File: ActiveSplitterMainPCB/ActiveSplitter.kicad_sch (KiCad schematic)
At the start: 24 parts, among them J1 SMA_EDGE, J2 SMA_EDGE, J3 SMA_EDGE, J4 SMA_EDGE, J5 SMA_EDGE, J6 Conn_01x28_Pin, J7 Conn_01x28_Pin, J8 Conn_01x12_Pin, J9 Conn_01x12_Pin, U1 PSA4-5043

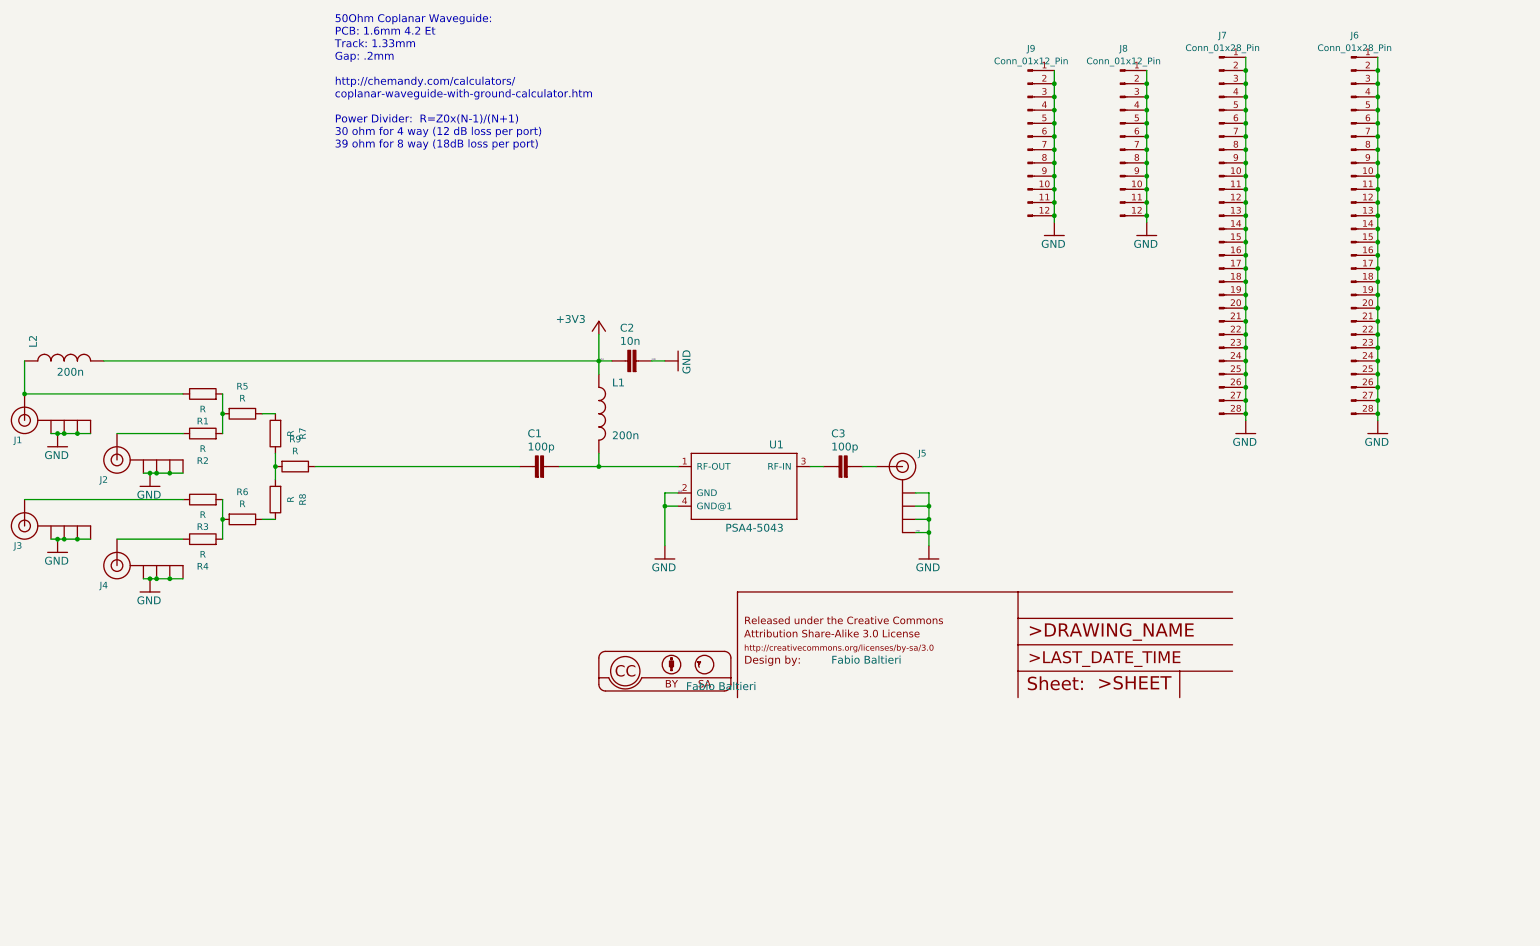
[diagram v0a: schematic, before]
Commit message: add termination resistors, PDF and SVG outputs for viewing
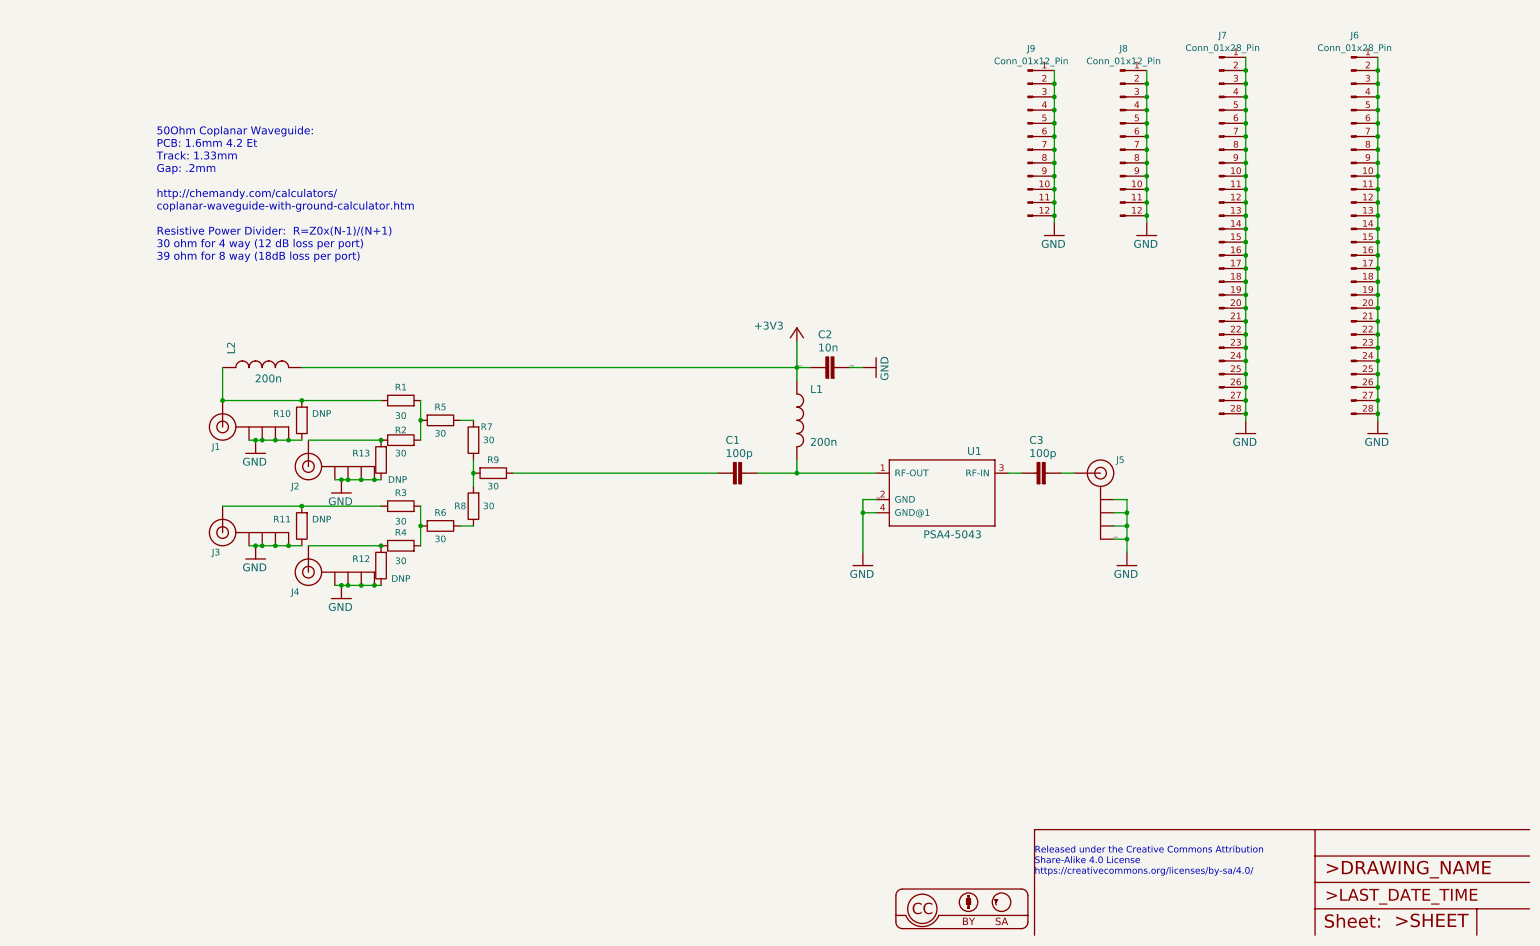
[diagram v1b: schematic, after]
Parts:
- added R10, R11, R12, R13: DNP, Resistor_SMD:R_0603_1608Metric_Pad0.98x0.95mm_HandSolder, symbol Device:R
- R1, R2, R3, R4, R5, R6, R7, R8, R9: value R -> 30
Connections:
- net GND: now also R10.1, R11.1, R12.1, R13.1
- net at J1.1 (SIGNAL), L2.1, R1.1: now also R10.2
- net at J3.1 (SIGNAL), R3.1: now also R11.2
- net at J4.1 (SIGNAL), R4.1: now also R12.2
- net at J2.1 (SIGNAL), R2.1: now also R13.2
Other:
- note added: "50Ohm Coplanar Waveguide: PCB: 1.6mm 4.2 Et Track: 1.33mm Gap: .2mm http://chemandy.com/calculators/ coplanar-waveguide-with-ground-calculator.htm Resistive Power Divider: R=Z0x(N-1)/(N+1) 30 ohm for 4 way (12 dB loss per port) 39 ohm for 8 way (18dB loss per port)"
- note added: "Released under the Creative Commons Attribution Share-Alike 4.0 License https://creativecommons.org/licenses/by-sa/4.0/"
- note removed: "50Ohm Coplanar Waveguide: PCB: 1.6mm 4.2 Et Track: 1.33mm Gap: .2mm http://chemandy.com/calculators/ coplanar-waveguide-with-ground-calculator.htm Power Divider: R=Z0x(N-1)/(N+1) 30 ohm for 4 way (12 dB loss per port) 39 ohm for 8 way (18dB loss per port)"
- moved on the sheet: C1, C2, C3, J1, J2, J3, J4, J5, L1, L2, R1, R2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

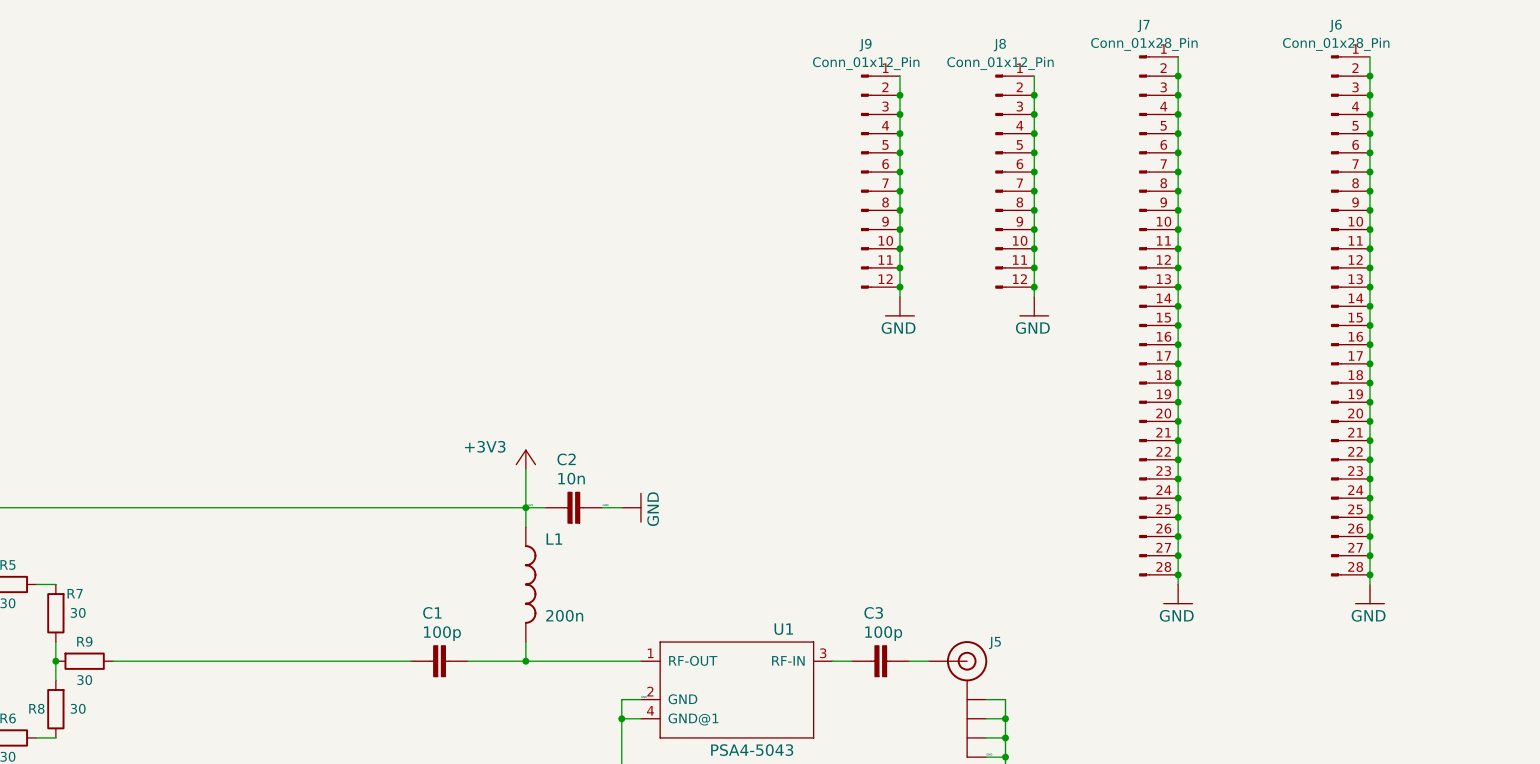
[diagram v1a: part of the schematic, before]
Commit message: Reduced output SMA spacing to 17mm to match USB hub.  Added pad for external 3V supply.
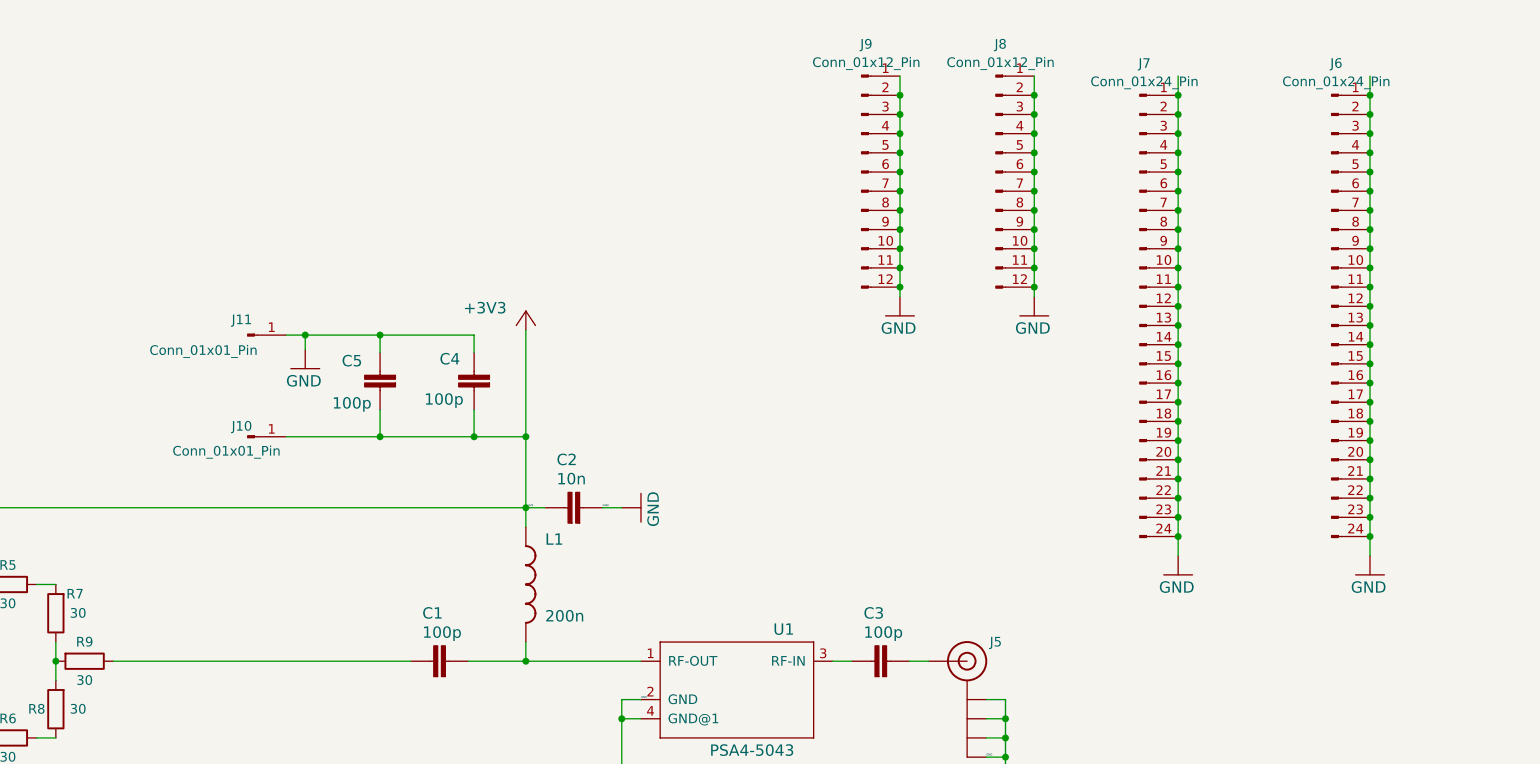
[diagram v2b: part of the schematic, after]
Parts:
- added C4, C5: 100p, Capacitor_SMD:C_0603_1608Metric_Pad1.08x0.95mm_HandSolder, symbol ActiveSplitter-eagle-import:C-EUC0603
- added J10, J11: Conn_01x01_Pin, Connector_Wire:SolderWire-0.75sqmm_1x01_D1.25mm_OD2.3mm, symbol Connector:Conn_01x01_Pin
- J6, J7: value Conn_01x28_Pin -> Conn_01x24_Pin; footprint Connector_PinHeader_2.54mm:PinHeader_1x28_P2.54mm_Vertical -> Connector_PinHeader_2.54mm:PinHeader_1x24_P2.54mm_Vertical; symbol Connector:Conn_01x28_Pin -> Connector:Conn_01x24_Pin
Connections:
- net +3V3: now also C4.1, C5.1, J10.1 (Pin_1)
- net GND: now also C4.2, C5.2, J11.1 (Pin_1); no longer J6.25 (Pin_25), J6.26 (Pin_26), J6.27 (Pin_27), J6.28 (Pin_28), J7.25 (Pin_25), J7.26 (Pin_26), J7.27 (Pin_27), J7.28 (Pin_28)

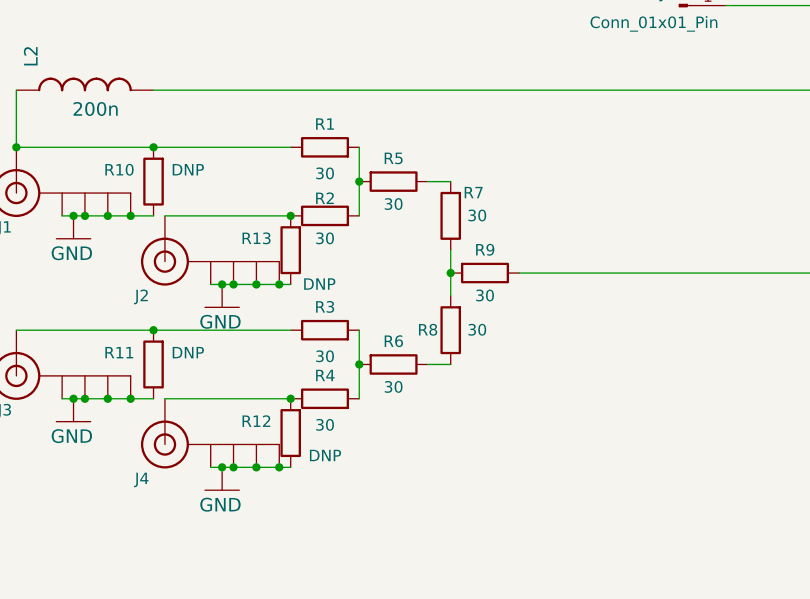
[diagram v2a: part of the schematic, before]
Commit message: fix resistor values
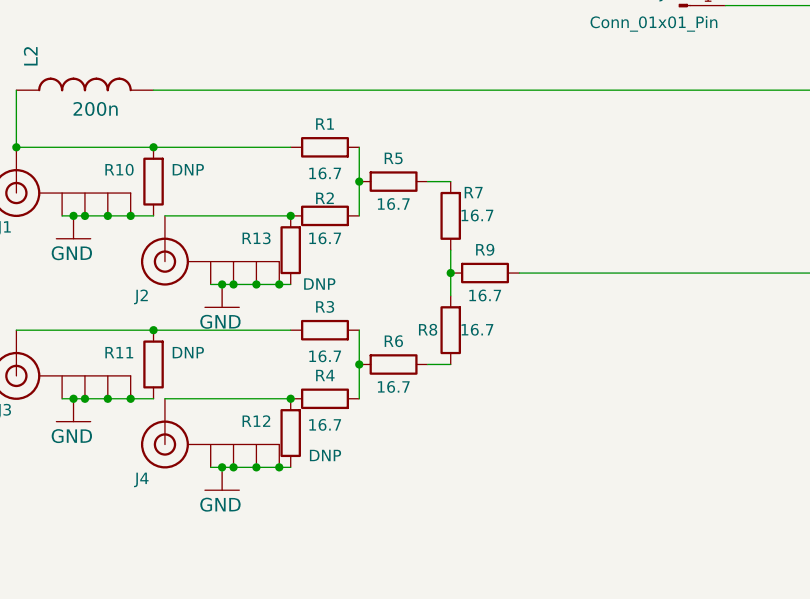
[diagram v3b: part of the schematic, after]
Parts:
- R1, R2, R3, R4, R5, R6, R7, R8, R9: value 30 -> 16.7
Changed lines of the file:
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@@
       (effects (font (size 1.27 1.27)))
     )
-    (property "Value" "30" (at 96.52 123.19 90)
+    (property "Value" "16.7" (at 96.52 123.19 90)
       (effects (font (size 1.27 1.27)))
     )
@@
       (effects (font (size 1.27 1.27)))
     )
-    (property "Value" "30" (at 95.6564 114.3 0)
+    (property "Value" "16.7" (at 95.6564 114.3 0)
       (effects (font (size 1.27 1.27)))
     )
@@
       (effects (font (size 1.27 1.27)))
     )
-    (property "Value" "30" (at 95.6564 127 0)
+    (property "Value" "16.7" (at 95.6564 127 0)
       (effects (font (size 1.27 1.27)))
     )
@@
       (effects (font (size 1.27 1.27)))
     )
-    (property "Value" "30" (at 86.36 113.03 90)
+    (property "Value" "16.7" (at 86.36 113.03 90)
       (effects (font (size 1.27 1.27)))
     )
@@
       (effects (font (size 1.27 1.27)))
     )
-    (property "Value" "30" (at 78.74 109.6264 90)
+    (property "Value" "16.7" (at 78.74 109.6264 90)
       (effects (font (size 1.27 1.27)))
     )
@@
       (effects (font (size 1.27 1.27)))
     )
-    (property "Value" "30" (at 78.74 129.9464 90)
+    (property "Value" "16.7" (at 78.74 129.9464 90)
       (effects (font (size 1.27 1.27)))
     )
@@
       (effects (font (size 1.27 1.27)))
     )
-    (property "Value" "30" (at 78.74 137.5664 90)
+    (property "Value" "16.7" (at 78.74 137.5664 90)
       (effects (font (size 1.27 1.27)))
     )
@@
       (effects (font (size 1.27 1.27)))
     )
-    (property "Value" "30" (at 78.74 116.84 90)
+    (property "Value" "16.7" (at 78.74 116.84 90)
       (effects (font (size 1.27 1.27)))
     )
@@
       (effects (font (size 1.27 1.27)))
     )
-    (property "Value" "30" (at 86.36 133.35 90)
+    (property "Value" "16.7" (at 86.36 133.35 90)
       (effects (font (size 1.27 1.27)))
     )
